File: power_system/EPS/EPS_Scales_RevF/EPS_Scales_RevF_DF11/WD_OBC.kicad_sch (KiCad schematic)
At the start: 37 parts, among them J9 Conn_01x04, U11 TLV1704

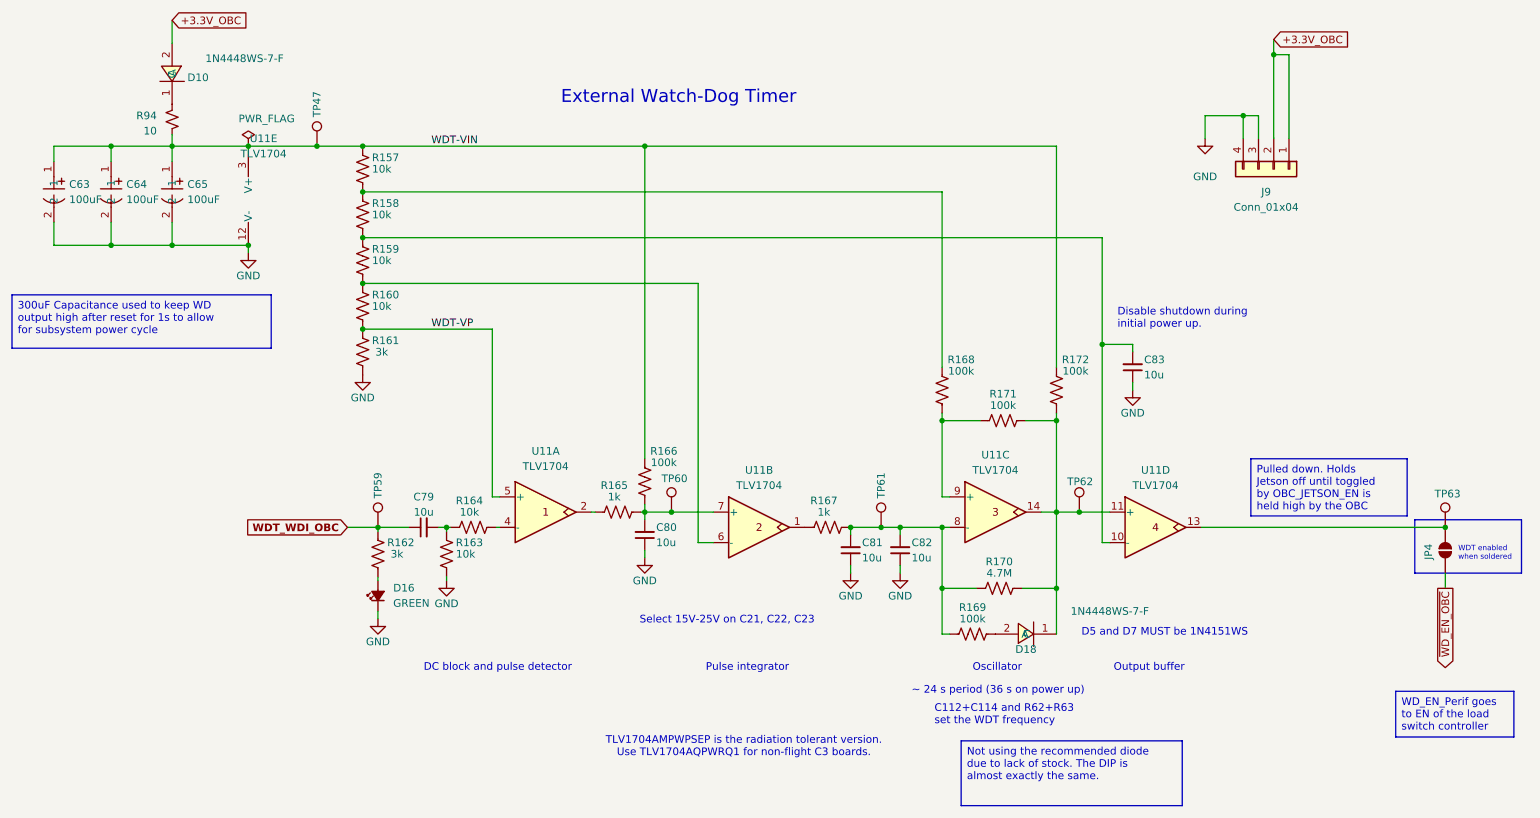
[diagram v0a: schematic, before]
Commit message: Completed EPS REV F / Viking 1-C PCB
Fixed minor issue with the extra resistor for the EN line VD, and added temperature sensors for each subsystem.
Also, the JPL logo is back!
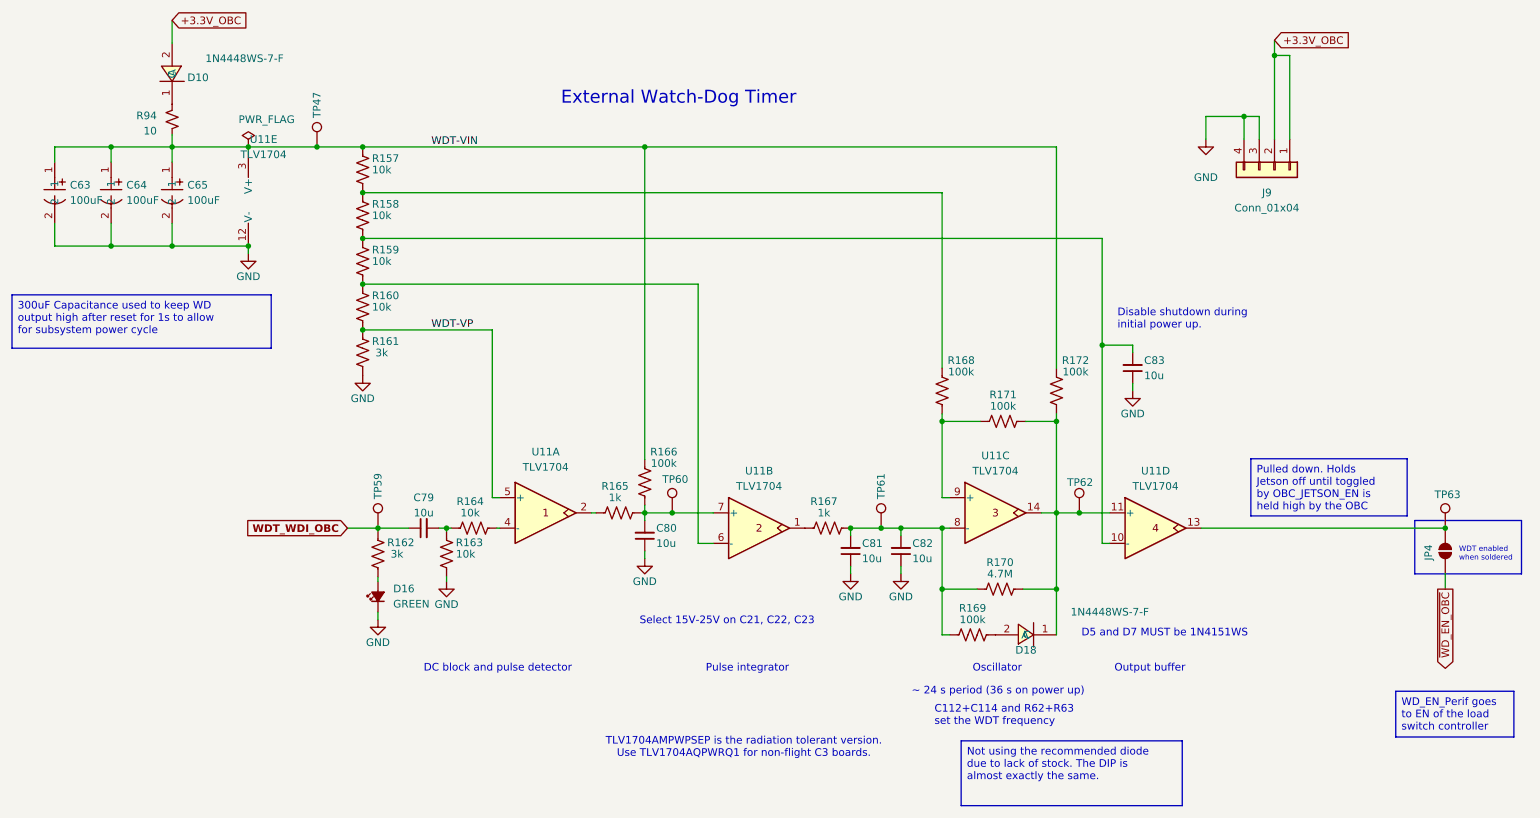
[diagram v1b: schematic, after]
